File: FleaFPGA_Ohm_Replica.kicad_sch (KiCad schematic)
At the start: 4 parts

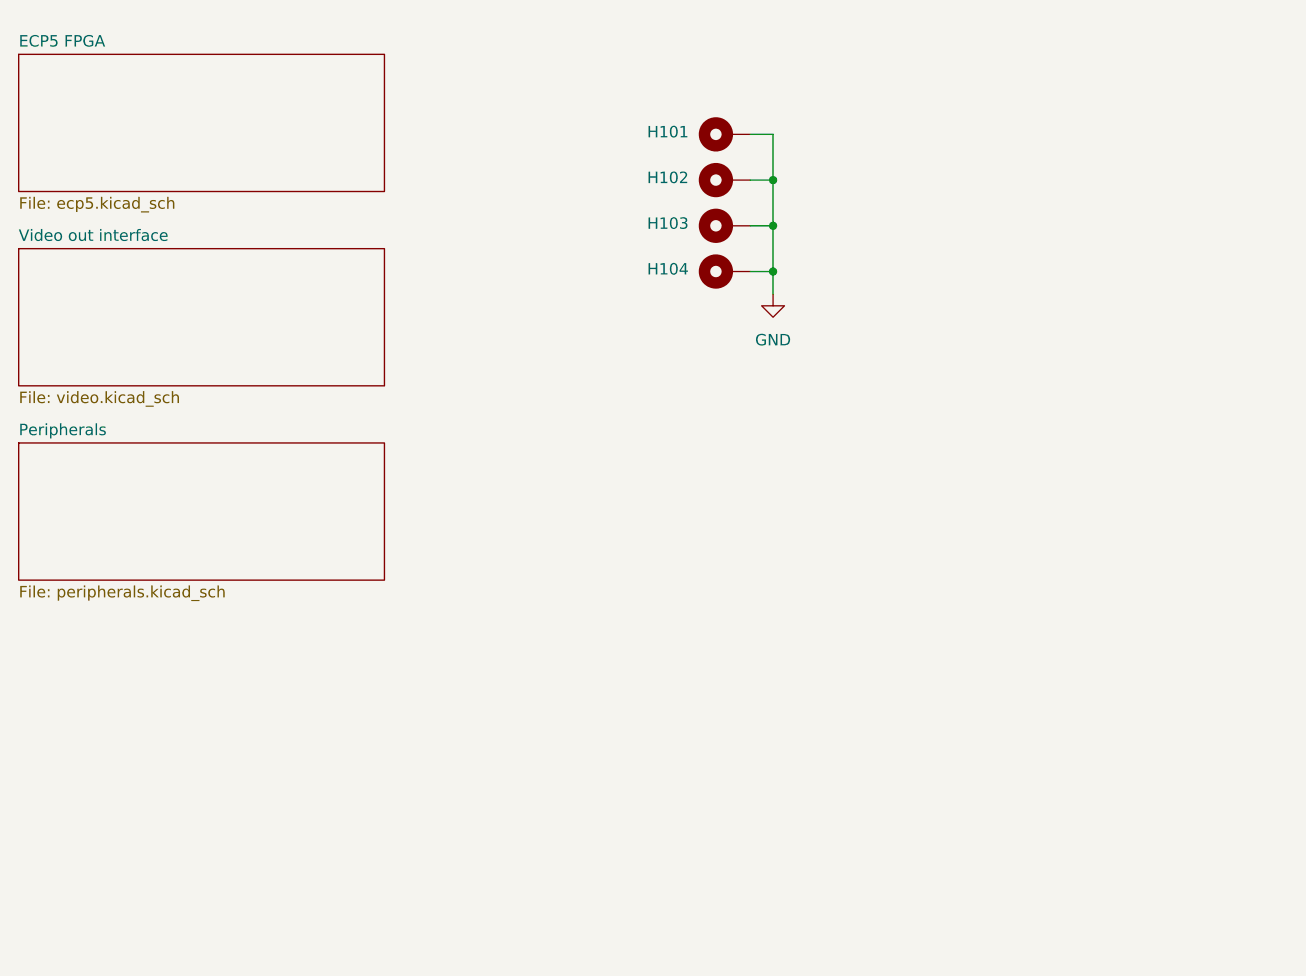
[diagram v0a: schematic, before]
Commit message: Towards routing RAM
 - Moved the RAM to its own sheet
 - Use the ECP5 prefix to capture impedance controlled traces
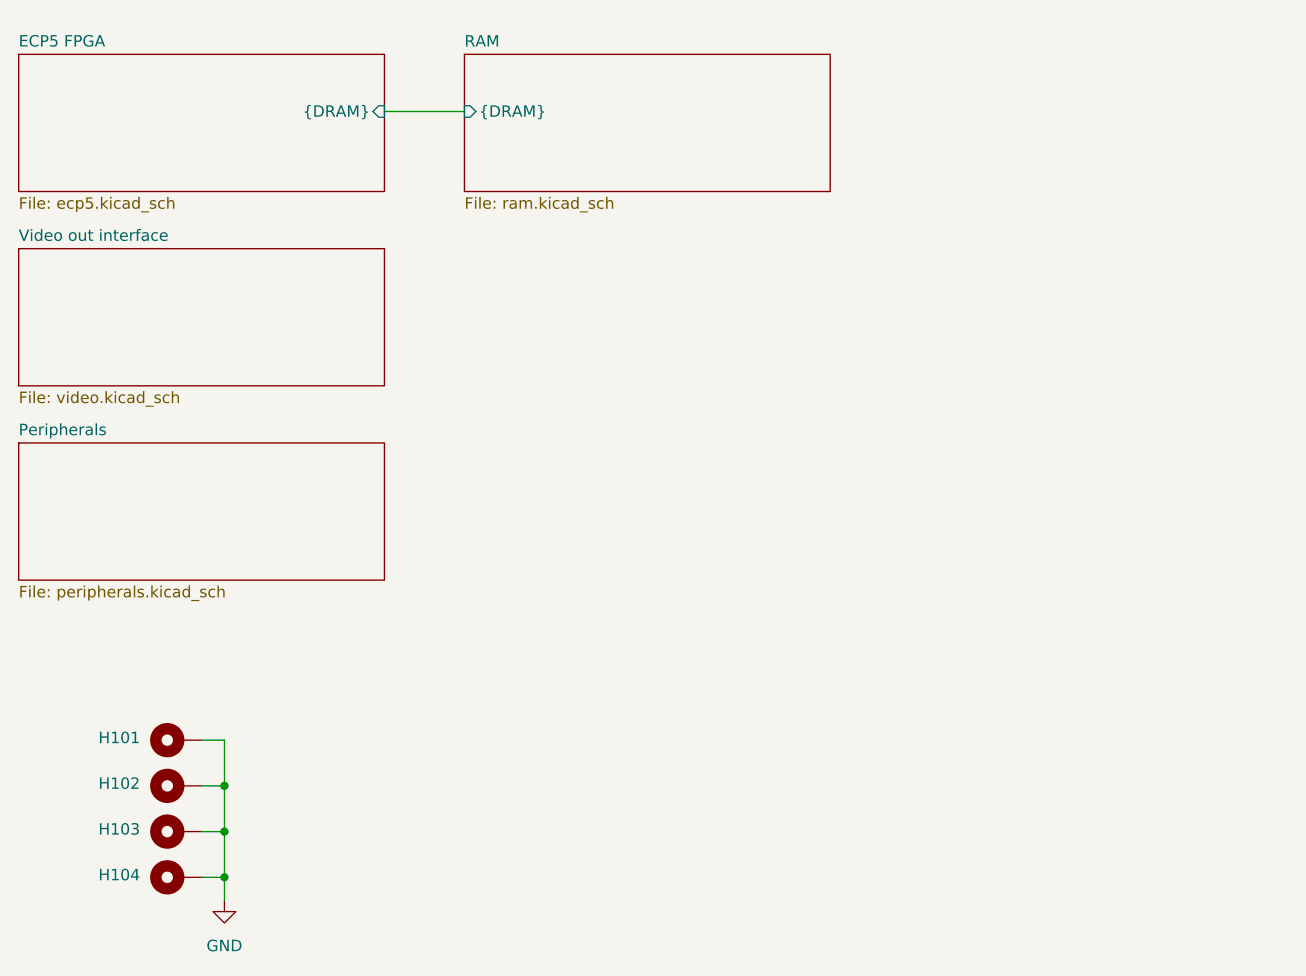
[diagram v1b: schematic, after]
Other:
- added sheet RAM (ram.kicad_sch)
- sheet ECP5 FPGA ports: added {DRAM}; removed none
- moved on the sheet: H101, H102, H103, H104
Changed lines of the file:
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@@
 	(paper "A4")
 	(junction
-		(at 120.65 53.34)
+		(at 59.69 120.65)
 		(diameter 0)
 		(color 0 0 0 0)
 	)
 	(junction
-		(at 120.65 48.26)
+		(at 59.69 115.57)
 		(diameter 0)
 		(color 0 0 0 0)
 	)
 	(junction
-		(at 120.65 43.18)
+		(at 59.69 110.49)
 		(diameter 0)
 		(color 0 0 0 0)
@@
 	(wire
 		(pts
-			(xy 120.65 38.1) (xy 120.65 43.18)
-		)
-		(stroke
-			(width 0)
-			(type default)
-		)
-	)
-	(wire
-		(pts
-			(xy 118.11 48.26) (xy 120.65 48.26)
-		)
-		(stroke
-			(width 0)
-			(type default)
-		)
-	)
-	(wire
-		(pts
-			(xy 120.65 48.26) (xy 120.65 53.34)
-		)
-		(stroke
-			(width 0)
-			(type default)
-		)
-	)
-	(wire
-		(pts
-			(xy 118.11 38.1) (xy 120.65 38.1)
-		)
-		(stroke
-			(width 0)
-			(type default)
-		)
-	)
-	(wire
-		(pts
-			(xy 118.11 43.18) (xy 120.65 43.18)
-		)
-		(stroke
-			(width 0)
-			(type default)
-		)
-	)
-	(wire
-		(pts
-			(xy 120.65 53.34) (xy 120.65 55.88)
-		)
-		(stroke
-			(width 0)
-			(type default)
-		)
-	)
-	(wire
-		(pts
-			(xy 120.65 43.18) (xy 120.65 48.26)
-		)
-		(stroke
-			(width 0)
-			(type default)
-		)
-	)
-	(wire
-		(pts
-			(xy 118.11 53.34) (xy 120.65 53.34)
+			(xy 59.69 105.41) (xy 59.69 110.49)
+		)
+		(stroke
+			(width 0)
+			(type default)
+		)
+	)
+	(wire
+		(pts
+			(xy 57.15 115.57) (xy 59.69 115.57)
+		)
+		(stroke
+			(width 0)
+			(type default)
+		)
+	)
+	(wire
+		(pts
+			(xy 59.69 115.57) (xy 59.69 120.65)
+		)
+		(stroke
+			(width 0)
+			(type default)
+		)
+	)
+	(wire
+		(pts
+			(xy 77.47 35.56) (xy 86.36 35.56)
+		)
+		(stroke
+			(width 0)
+			(type default)
+		)
+	)
+	(wire
+		(pts
+			(xy 57.15 105.41) (xy 59.69 105.41)
+		)
+		(stroke
+			(width 0)
+			(type default)
+		)
+	)
+	(wire
+		(pts
+			(xy 57.15 110.49) (xy 59.69 110.49)
+		)
+		(stroke
+			(width 0)
+			(type default)
+		)
+	)
+	(wire
+		(pts
+			(xy 59.69 120.65) (xy 59.69 123.19)
+		)
+		(stroke
+			(width 0)
+			(type default)
+		)
+	)
+	(wire
+		(pts
+			(xy 59.69 110.49) (xy 59.69 115.57)
+		)
+		(stroke
+			(width 0)
+			(type default)
+		)
+	)
+	(wire
+		(pts
+			(xy 57.15 120.65) (xy 59.69 120.65)
 		)
 		(stroke
@@
 	(symbol
 		(lib_id "Mechanical:MountingHole_Pad")
-		(at 115.57 48.26 90)
+		(at 54.61 115.57 90)
 		(unit 1)
 		(exclude_from_sim yes)
@@
 		(dnp no)
 		(property "Reference" "H103"
-			(at 108.966 48.006 90)
+			(at 48.006 115.316 90)
 			(effects
 				(font
@@
 		)
 		(property "Value" "MountingHole_Pad"
-			(at 114.3 44.45 90)
+			(at 53.34 111.76 90)
 			(effects
 				(font
@@
 		)
 		(property "Footprint" "MountingHole:MountingHole_2.7mm_M2.5_Pad"
-			(at 115.57 48.26 0)
+			(at 54.61 115.57 0)
 			(effects
 				(font
@@
 		)
 		(property "Datasheet" "~"
-			(at 115.57 48.26 0)
+			(at 54.61 115.57 0)
 			(effects
 				(font
@@
 		)
 		(property "Description" "Mounting Hole with connection"
-			(at 115.57 48.26 0)
+			(at 54.61 115.57 0)
 			(effects
 				(font
@@
 	(symbol
 		(lib_id "power:GND")
-		(at 120.65 55.88 0)
+		(at 59.69 123.19 0)
 		(unit 1)
 		(exclude_from_sim no)
@@
 		(fields_autoplaced yes)
 		(property "Reference" "#PWR0101"
-			(at 120.65 62.23 0)
+			(at 59.69 129.54 0)
 			(effects
 				(font
@@
 		)
 		(property "Value" "GND"
-			(at 120.65 60.96 0)
+			(at 59.69 128.27 0)
 			(effects
 				(font
@@
 		)
 		(property "Footprint" ""
-			(at 120.65 55.88 0)
+			(at 59.69 123.19 0)
 			(effects
 				(font
@@
 		)
 		(property "Datasheet" ""
-			(at 120.65 55.88 0)
+			(at 59.69 123.19 0)
 			(effects
 				(font
@@
 		)
 		(property "Description" "Power symbol creates a global label with name \"GND\" , ground"
-			(at 120.65 55.88 0)
+			(at 59.69 123.19 0)
 			(effects
 				(font
@@
 	(symbol
 		(lib_id "Mechanical:MountingHole_Pad")
-		(at 115.57 38.1 90)
+		(at 54.61 105.41 90)
 		(unit 1)
 		(exclude_from_sim yes)
@@
 		(dnp no)
 		(property "Reference" "H101"
-			(at 108.966 37.846 90)
+			(at 48.006 105.156 90)
 			(effects
 				(font
@@
 		)
 		(property "Value" "MountingHole_Pad"
-			(at 114.3 34.29 90)
+			(at 53.34 101.6 90)
 			(effects
 				(font
@@
 		)
 		(property "Footprint" "MountingHole:MountingHole_2.7mm_M2.5_Pad"
-			(at 115.57 38.1 0)
+			(at 54.61 105.41 0)
 			(effects
 				(font
@@
 		)
 		(property "Datasheet" "~"
-			(at 115.57 38.1 0)
+			(at 54.61 105.41 0)
 			(effects
 				(font
@@
 		)
 		(property "Description" "Mounting Hole with connection"
-			(at 115.57 38.1 0)
+			(at 54.61 105.41 0)
 			(effects
 				(font
@@
 	(symbol
 		(lib_id "Mechanical:MountingHole_Pad")
-		(at 115.57 53.34 90)
+		(at 54.61 120.65 90)
 		(unit 1)
 		(exclude_from_sim yes)
@@
 		(dnp no)
 		(property "Reference" "H104"
-			(at 108.966 53.086 90)
+			(at 48.006 120.396 90)
 			(effects
 				(font
@@
 		)
 		(property "Value" "MountingHole_Pad"
-			(at 114.3 49.53 90)
+			(at 53.34 116.84 90)
 			(effects
 				(font
@@
 		)
 		(property "Footprint" "MountingHole:MountingHole_2.7mm_M2.5_Pad"
-			(at 115.57 53.34 0)
+			(at 54.61 120.65 0)
 			(effects
 				(font
@@
 		)
 		(property "Datasheet" "~"
-			(at 115.57 53.34 0)
+			(at 54.61 120.65 0)
 			(effects
 				(font
@@
 		)
 		(property "Description" "Mounting Hole with connection"
-			(at 115.57 53.34 0)
+			(at 54.61 120.65 0)
 			(effects
 				(font
@@
 	(symbol
 		(lib_id "Mechanical:MountingHole_Pad")
-		(at 115.57 43.18 90)
+		(at 54.61 110.49 90)
 		(unit 1)
 		(exclude_from_sim yes)
@@
 		(dnp no)
 		(property "Reference" "H102"
-			(at 108.966 42.926 90)
+			(at 48.006 110.236 90)
 			(effects
 				(font
@@
 		)
 		(property "Value" "MountingHole_Pad"
-			(at 114.3 39.37 90)
+			(at 53.34 106.68 90)
 			(effects
 				(font
@@
 		)
 		(property "Footprint" "MountingHole:MountingHole_2.7mm_M2.5_Pad"
-			(at 115.57 43.18 0)
+			(at 54.61 110.49 0)
 			(effects
 				(font
@@
 		)
 		(property "Datasheet" "~"
-			(at 115.57 43.18 0)
+			(at 54.61 110.49 0)
 			(effects
 				(font
@@
 		)
 		(property "Description" "Mounting Hole with connection"
-			(at 115.57 43.18 0)
+			(at 54.61 110.49 0)
 			(effects
 				(font
@@
 			)
 		)
+		(pin "{DRAM}" input
+			(at 77.47 35.56 0)
+			(effects
+				(font
+					(size 1.27 1.27)
+				)
+				(justify right)
+			)
+		)
 		(instances
 			(project "FleaFPGA_Ohm_Replica"
@@
 				)
 			)
+		)
+	)
+	(sheet
+		(at 86.36 29.21)
+		(size 40.64 15.24)
+		(fields_autoplaced yes)
+		(stroke
+			(width 0.1524)
+			(type solid)
+		)
+		(fill
+			(color 0 0 0 0.0000)
+		)
+		(property "Sheetname" "RAM"
+			(at 86.36 28.4984 0)
+			(effects
+				(font
+					(size 1.27 1.27)
+				)
+				(justify left bottom)
+			)
+		)
+		(property "Sheetfile" "ram.kicad_sch"
+			(at 86.36 45.0346 0)
+			(effects
+				(font
+					(size 1.27 1.27)
+				)
+				(justify left top)
+			)
+		)
+		(pin "{DRAM}" input
+			(at 86.36 35.56 180)
+			(effects
+				(font
+					(size 1.27 1.27)
+				)
+				(justify left)
+			)
+		)
+		(instances
+			(project "FleaFPGA_Ohm_Replica"
+				(path "/234cb242-35b7-4c9f-a377-7513f8760142"
+					(page "5")
+				)
+			)

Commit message: First whole routing
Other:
- sheet Peripherals renamed Peripherals and Power
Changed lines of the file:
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@@
 			(color 0 0 0 0.0000)
 		)
-		(property "Sheetname" "Peripherals"
+		(property "Sheetname" "Peripherals and Power"
 			(at 36.83 71.6784 0)
 			(effects

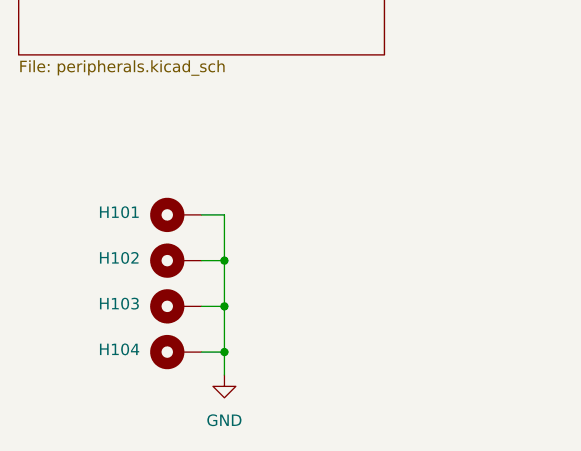
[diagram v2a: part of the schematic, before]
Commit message: Update some component values and complete MPN for BOM
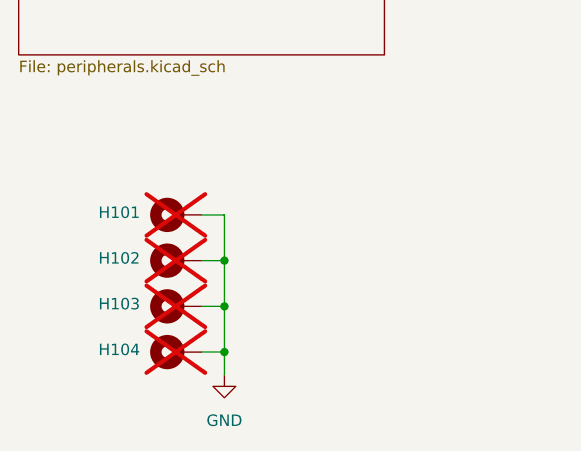
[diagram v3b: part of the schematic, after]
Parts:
- H101, H102, H103, H104: now not fitted
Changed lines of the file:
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@@
 		(in_bom no)
 		(on_board yes)
-		(dnp no)
+		(dnp yes)
 		(property "Reference" "H103"
 			(at 48.006 115.316 90)
@@
 		(in_bom no)
 		(on_board yes)
-		(dnp no)
+		(dnp yes)
 		(property "Reference" "H101"
 			(at 48.006 105.156 90)
@@
 		(in_bom no)
 		(on_board yes)
-		(dnp no)
+		(dnp yes)
 		(property "Reference" "H104"
 			(at 48.006 120.396 90)
@@
 		(in_bom no)
 		(on_board yes)
-		(dnp no)
+		(dnp yes)
 		(property "Reference" "H102"
 			(at 48.006 110.236 90)

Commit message: Minor fixes
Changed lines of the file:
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@@
 	(wire
 		(pts
-			(xy 77.47 35.56) (xy 86.36 35.56)
+			(xy 128.27 57.15) (xy 137.16 57.15)
 		)
 		(stroke
@@
 	)
 	(sheet
-		(at 36.83 72.39)
+		(at 87.63 27.94)
 		(size 40.64 15.24)
 		(fields_autoplaced yes)
@@
 		)
 		(property "Sheetname" "Peripherals and Power"
-			(at 36.83 71.6784 0)
+			(at 87.63 27.2284 0)
 			(effects
 				(font
@@
 		)
 		(property "Sheetfile" "peripherals.kicad_sch"
-			(at 36.83 88.2146 0)
+			(at 87.63 43.7646 0)
 			(effects
 				(font
@@
 	)
 	(sheet
-		(at 36.83 29.21)
+		(at 87.63 50.8)
 		(size 40.64 15.24)
 		(fields_autoplaced yes)
@@
 		)
 		(property "Sheetname" "ECP5 FPGA"
-			(at 36.83 28.4984 0)
+			(at 87.63 50.0884 0)
 			(effects
 				(font
@@
 		)
 		(property "Sheetfile" "ecp5.kicad_sch"
-			(at 36.83 45.0346 0)
+			(at 87.63 66.6246 0)
 			(effects
 				(font
@@
 		)
 		(pin "{DRAM}" input
-			(at 77.47 35.56 0)
+			(at 128.27 57.15 0)
 			(effects
 				(font
@@
 	)
 	(sheet
-		(at 86.36 29.21)
+		(at 137.16 50.8)
 		(size 40.64 15.24)
 		(fields_autoplaced yes)
@@
 		)
 		(property "Sheetname" "RAM"
-			(at 86.36 28.4984 0)
+			(at 137.16 50.0884 0)
 			(effects
 				(font
@@
 		)
 		(property "Sheetfile" "ram.kicad_sch"
-			(at 86.36 45.0346 0)
+			(at 137.16 66.6246 0)
 			(effects
 				(font
@@
 		)
 		(pin "{DRAM}" input
-			(at 86.36 35.56 180)
-			(effects
-				(font
+			(at 137.16 57.15 180)
+			(effects
+				(font
